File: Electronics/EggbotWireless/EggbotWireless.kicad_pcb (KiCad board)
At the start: 2 copper layers, 118 x 40 mm, 77 parts, among them J1 BATT, J2 Conn_01x03_Male, J3 USB_B_Micro, J4 AVR-ISP-6, J5 Conn_01x03_Female, J6 Conn_01x05_Male, M1 , M2 , M3 Motor_Servo, Q1 FDD8447L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

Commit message: fix some power issues
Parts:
- added C17: 10uF, Capacitor_SMD:C_0805_2012Metric_Pad1.15x1.40mm_HandSolder, F.Cu at (117.7, 60.9)
- added D4: SSB43L, Diode_SMD:D_SMB_Handsoldering, F.Cu at (113.2, 56.3)
- D1: value SK24 -> SSB43L
- D2: value SK84 -> SSB43L
- JP1, JP2, JP3: value (none) -> SolderJumper_2_Bridged; footprint Jumper:SolderJumper-2_P1.3mm_Open_Pad1.0x1.5mm -> Jumper:SolderJumper-2_P1.3mm_Bridged_Pad1.0x1.5mm
- Q1: value FDD8447L -> FDD8800
- Q3: value AOD403 -> IRLML6402; footprint Package_TO_SOT_SMD:TO-252-2 -> Package_TO_SOT_SMD:SOT-23
- R15: value 0.006 -> 0.008
- R16: value 9.1K -> 8.45K
- R20, R22, R6: value 100K -> 10K
- moved Q3 2.96 mm to (112.1, 60.8)
- moved D2 0.38 mm to (114.2, 47.2)
- moved JP2 0.05 mm to (43.1, 38.9)
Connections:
- Q3 pad 2: BATT -> Net-(D4-Pad1)
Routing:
- net Net-(D2-Pad1): track 27.2 -> 34.7 mm
- net BATT: track 57.9 -> 65.2 mm
- net VBUS: track 53.4 -> 60.4 mm
- net Net-(D4-Pad1): track 0.00 -> 4.29 mm, vias 0 -> 1
- net +5V: track 168.0 -> 169.9 mm, vias 2 -> 4
- net Net-(D1-Pad2): track 19.6 -> 20.1 mm, vias 1 -> 2
- net +12V: track 107.2 -> 107.7 mm, vias 0 -> 1
- net GND: vias 18 -> 19
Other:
- board text added: "Eggbot Wireless v1.3"
- board text removed: "Eggbot Wireless v1.2b"

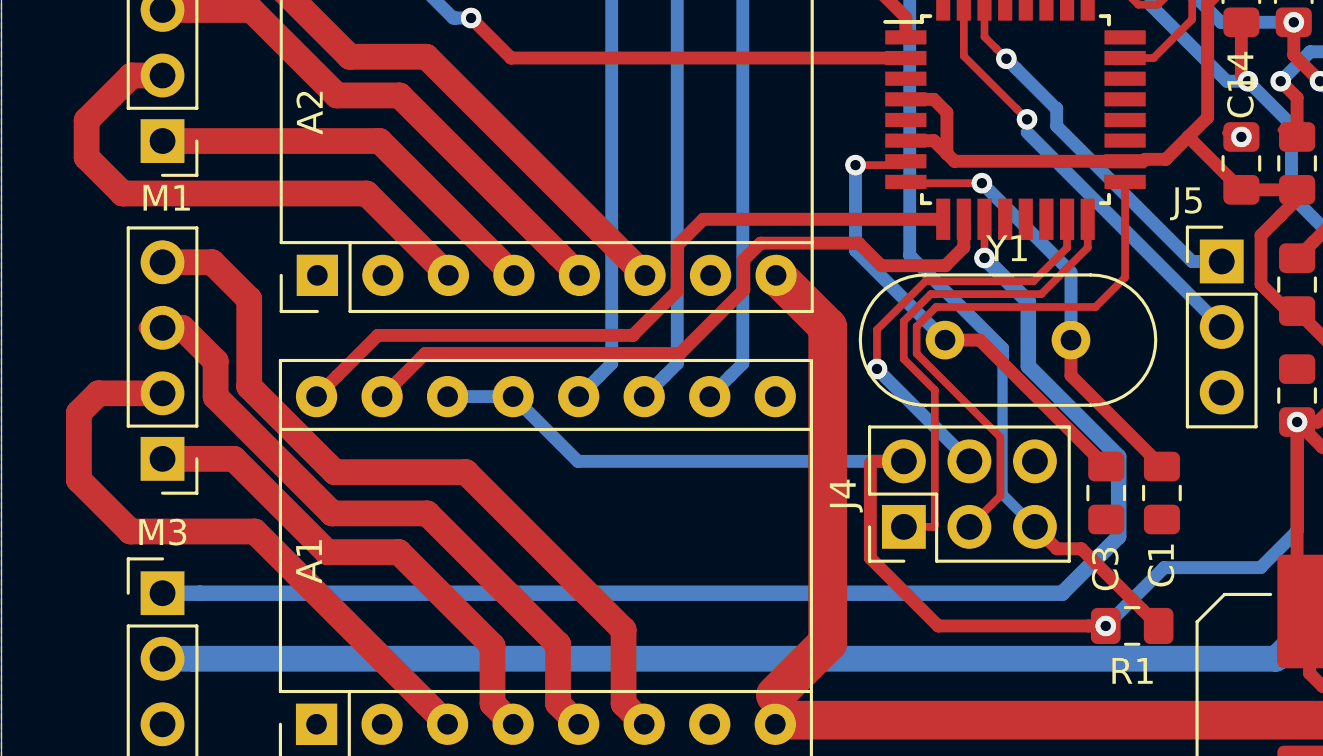
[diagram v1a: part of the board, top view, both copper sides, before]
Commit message: better crystal routing
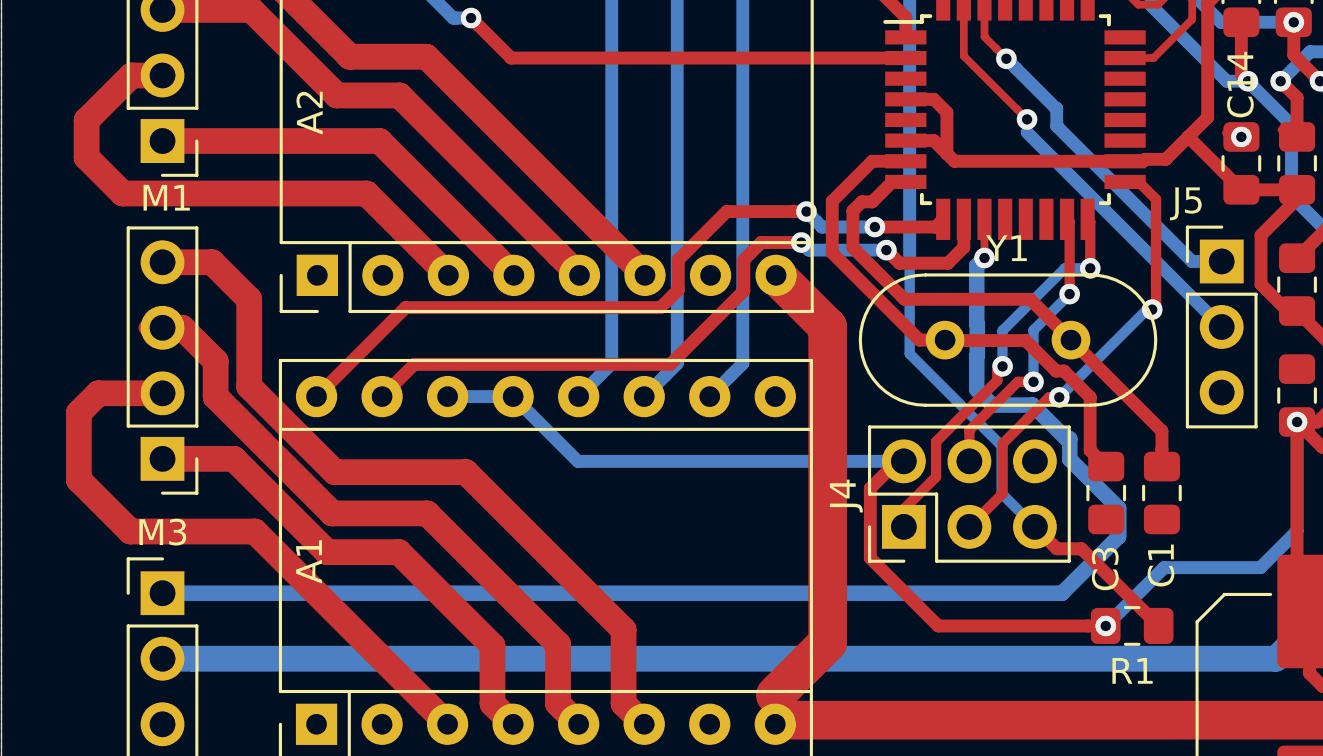
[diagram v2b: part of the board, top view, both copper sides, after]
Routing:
- net Net-(J4-Pad4): track 16.4 -> 11.4 mm, vias 1 -> 2
- net Net-(J4-Pad3): track 22.2 -> 17.5 mm, vias 0 -> 2
- net Net-(J4-Pad1): track 19.1 -> 15.5 mm, vias 0 -> 2
- net Net-(C1-Pad1): track 16.8 -> 20.2 mm, vias 1 -> 0
- net Net-(C3-Pad2): track 18.5 -> 20.8 mm, vias 1 -> 0
- net Net-(M3-Pad1): track 52.4 -> 53.7 mm
- net +3V3: track 246.0 -> 245.4 mm
- net DIR1: track 28.2 -> 28.3 mm, vias 0 -> 2
- net STEP1: vias 0 -> 2

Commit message: board v1.3
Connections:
- A1 pad 2: (no net) -> Net-(A1-Pad2)
- A1 pad 9: (no net) -> Net-(A1-Pad9)
- A2 pad 2: (no net) -> Net-(A2-Pad2)
- A2 pad 9: (no net) -> Net-(A2-Pad9)
- J3 pad 4: (no net) -> Net-(J3-Pad4)
- SW1 pad 3: (no net) -> Net-(SW1-Pad3)
- U2 pad 12: (no net) -> Net-(U2-Pad12)
- U2 pad 13: (no net) -> Net-(U2-Pad13)
- U2 pad 14: (no net) -> Net-(U2-Pad14)
- U2 pad 19: (no net) -> Net-(U2-Pad19)
- U2 pad 20: (no net) -> Net-(U2-Pad20)
- U2 pad 22: (no net) -> Net-(U2-Pad22)
- U2 pad 24: (no net) -> Net-(U2-Pad24)
- U2 pad 25: (no net) -> Net-(U2-Pad25)
- U2 pad 26: (no net) -> Net-(U2-Pad26)
- U2 pad 32: (no net) -> Net-(U2-Pad32)
- U3 pad 4: (no net) -> Net-(U3-Pad4)
- U5 pad 10: (no net) -> Net-(U5-Pad10)
- U5 pad 11: (no net) -> Net-(U5-Pad11)
- U5 pad 13: (no net) -> Net-(U5-Pad13)
- U5 pad 14: (no net) -> Net-(U5-Pad14)
- U5 pad 19: (no net) -> Net-(U5-Pad19)
- U5 pad 22: (no net) -> Net-(U5-Pad22)
- U5 pad 23: (no net) -> Net-(U5-Pad23)
- U5 pad 27: (no net) -> Net-(U5-Pad27)
- U5 pad 28: (no net) -> Net-(U5-Pad28)
- U5 pad 6: (no net) -> Net-(U5-Pad6)
- U5 pad 9: (no net) -> Net-(U5-Pad9)
- U7 pad 10: (no net) -> Net-(U7-Pad10)
- U7 pad 11: (no net) -> Net-(U7-Pad11)
- U7 pad 12: (no net) -> Net-(U7-Pad12)
- U7 pad 13: (no net) -> Net-(U7-Pad13)
- U7 pad 14: (no net) -> Net-(U7-Pad14)
- U7 pad 4: (no net) -> Net-(U7-Pad4)
- U7 pad 5: (no net) -> Net-(U7-Pad5)
- U7 pad 9: (no net) -> Net-(U7-Pad9)

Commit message: make inductor 6.8uH
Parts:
- L1: value 3.3uH -> 6.8uH
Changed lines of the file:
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@@
       (effects (font (size 1 1) (thickness 0.15)))
     )
-    (fp_text value 3.3uH (at 0 4.45) (layer F.Fab)
+    (fp_text value 6.8uH (at 0 4.45) (layer F.Fab)
       (effects (font (size 1 1) (thickness 0.15)))
     )

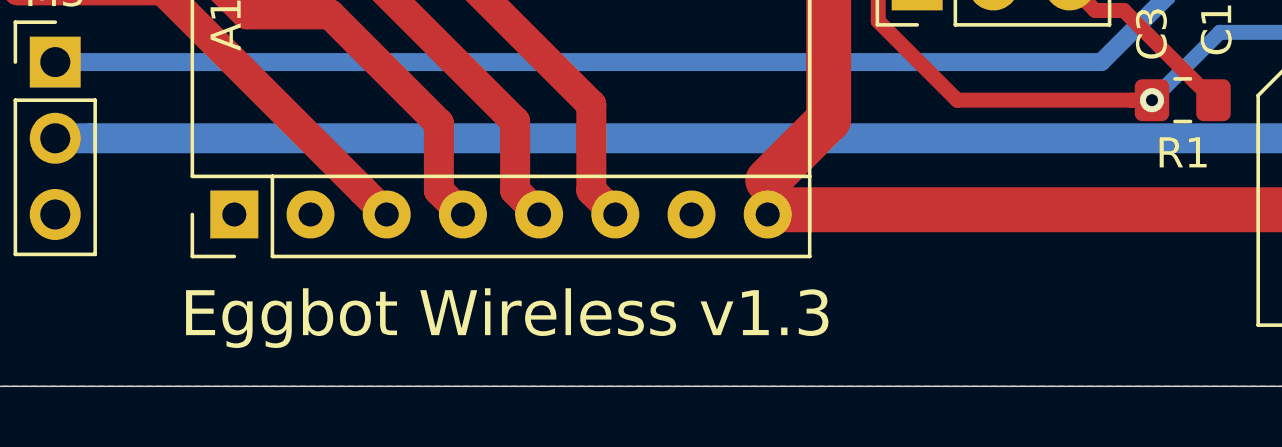
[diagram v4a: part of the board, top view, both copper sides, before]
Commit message: v1.3f some changes to the schematic
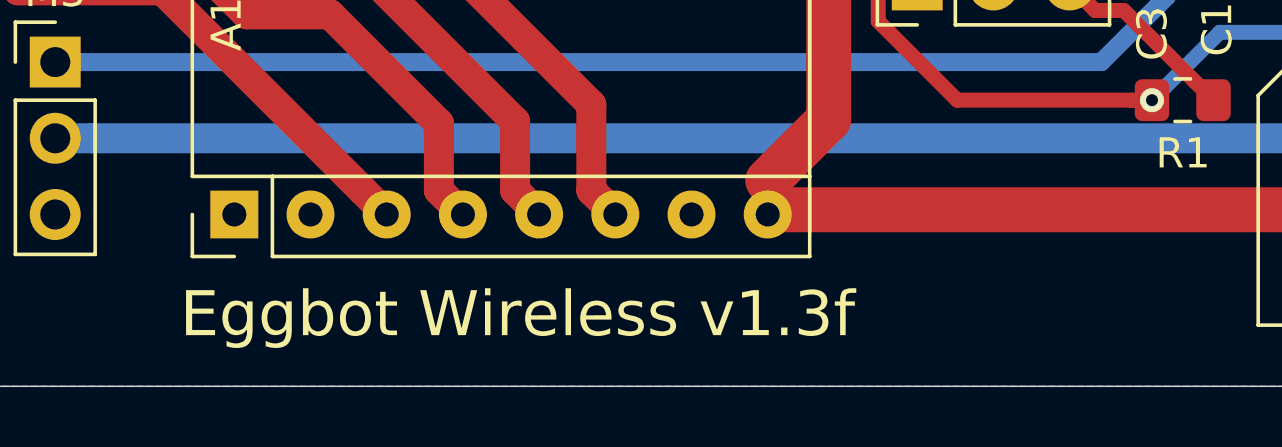
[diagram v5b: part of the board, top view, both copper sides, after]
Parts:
- R21: value 330 -> 510
- R27: value 3K -> 2.2K
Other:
- board text added: "Eggbot Wireless v1.3f"
- board text removed: "Eggbot Wireless v1.3"
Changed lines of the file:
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@@
-(kicad_pcb (version 20171130) (host pcbnew 5.1.2-5.1.2)
+(kicad_pcb (version 20171130) (host pcbnew 5.1.2-1.fc30)
   (general
     (thickness 1.6)
@@
       (effects (font (size 1 1) (thickness 0.15)))
     )
-    (fp_text value 3K (at 0 1.65 90) (layer F.Fab)
+    (fp_text value 2.2K (at 0 1.65 90) (layer F.Fab)
       (effects (font (size 1 1) (thickness 0.15)))
     )
@@
       (effects (font (size 1 1) (thickness 0.15)))
     )
-    (fp_text value 330 (at 0 1.65) (layer F.Fab)
+    (fp_text value 510 (at 0 1.65) (layer F.Fab)
       (effects (font (size 1 1) (thickness 0.15)))
     )
@@
   (gr_line (start 137.364 37.528) (end 137.364 77.528) (layer Edge.Cuts) (width 0.05))
   (gr_line (start 19.364 37.528) (end 137.364 37.528) (layer Edge.Cuts) (width 0.05))
-  (gr_text "Eggbot Wireless v1.3" (at 29.764 75.128) (layer F.SilkS)
+  (gr_text "Eggbot Wireless v1.3f" (at 29.764 75.128) (layer F.SilkS)
     (effects (font (size 1.5 1.5) (thickness 0.3)) (justify left))
   )

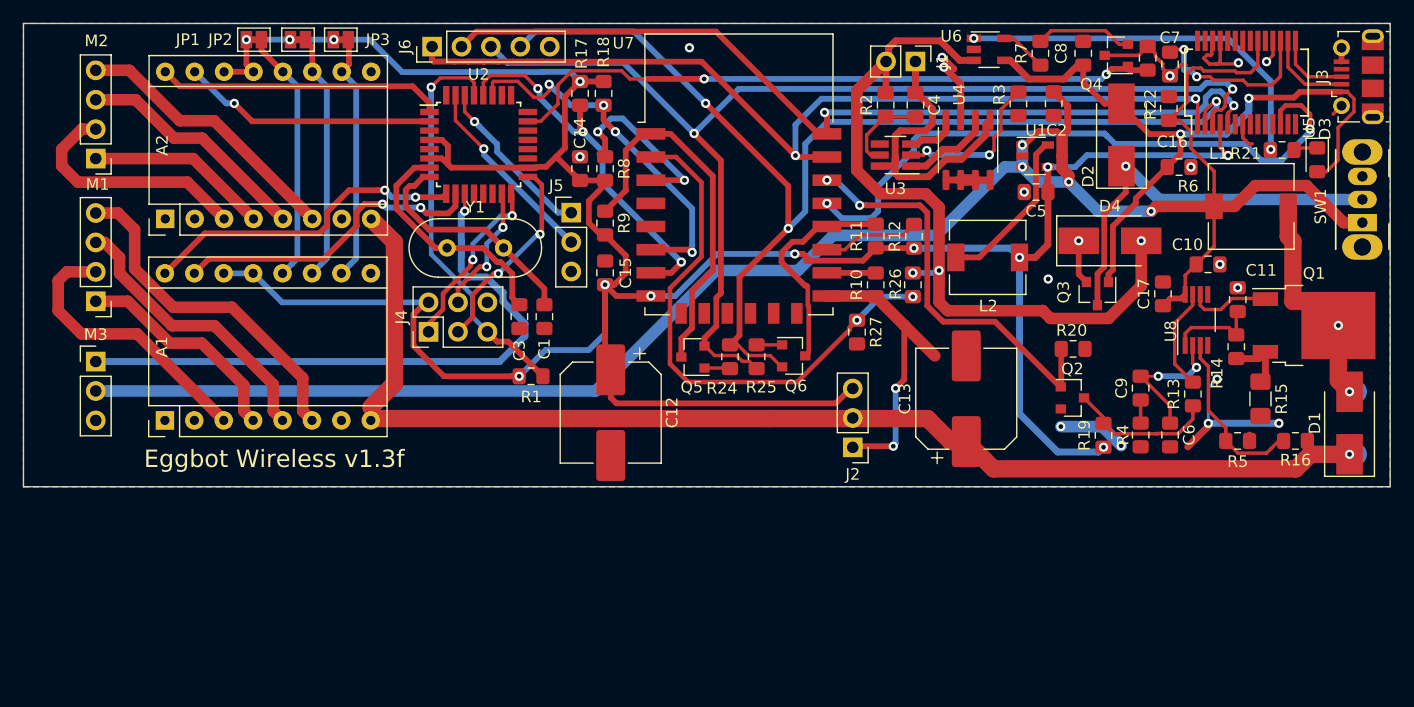
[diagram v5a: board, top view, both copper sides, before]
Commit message: add 5v boost schematic
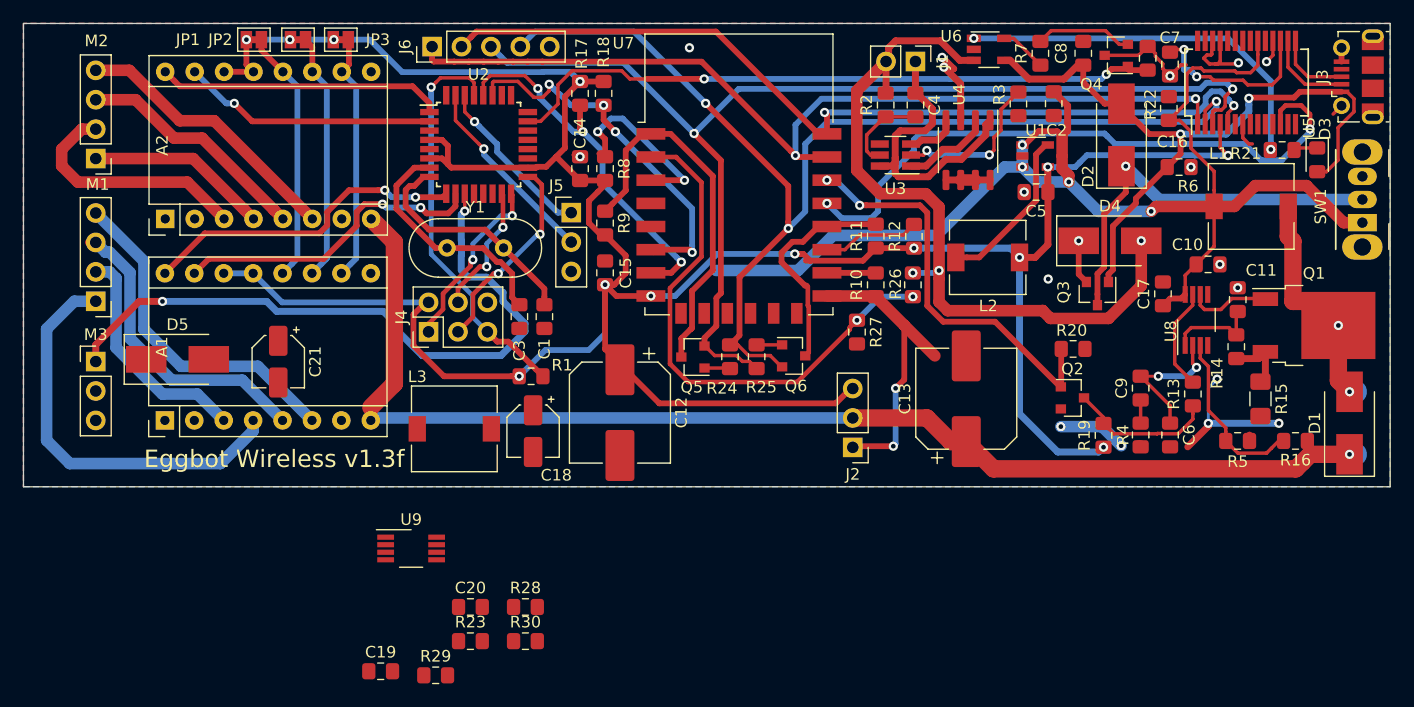
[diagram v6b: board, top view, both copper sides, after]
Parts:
- added C18: 10uF, Capacitor_SMD:CP_Elec_4x5.4, F.Cu at (63.4, 72.7)
- added C19: 22pF, Capacitor_SMD:C_0805_2012Metric_Pad1.15x1.40mm_HandSolder, F.Cu at (50.2, 93.5)
- added C20: 100nF, Capacitor_SMD:C_0805_2012Metric_Pad1.15x1.40mm_HandSolder, F.Cu at (58.0, 87.9)
- added C21: 10uF, Capacitor_SMD:CP_Elec_4x5.4, F.Cu at (41.4, 66.7)
- added D5: SSB43L, Diode_SMD:D_SMB_Handsoldering, F.Cu at (32.7, 66.5)
- added L3: 6.8uH, Inductor_SMD:L_7.3x7.3_H4.5, F.Cu at (56.6, 72.5)
- added R23: 50K, Resistor_SMD:R_0805_2012Metric_Pad1.15x1.40mm_HandSolder, F.Cu at (58.0, 90.9)
- added R28: 150K, Resistor_SMD:R_0805_2012Metric_Pad1.15x1.40mm_HandSolder, F.Cu at (62.7, 87.9)
- added R29: 200K, Resistor_SMD:R_0805_2012Metric_Pad1.15x1.40mm_HandSolder, F.Cu at (55.0, 93.8)
- added R30: 500, Resistor_SMD:R_0805_2012Metric_Pad1.15x1.40mm_HandSolder, F.Cu at (62.7, 90.9)
- added U9: LM2621, Package_SO:VSSOP-8_3.0x3.0mm_P0.65mm, F.Cu at (52.8, 82.9)
- moved C12 0.80 mm to (70.9, 71.1)
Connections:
- net 12V_SWITCH renamed PWR_SWITCH
- A1 pad 2: Net-(A1-Pad2) -> (no net)
- A1 pad 9: Net-(A1-Pad9) -> (no net)
- A2 pad 2: Net-(A2-Pad2) -> (no net)
- A2 pad 9: Net-(A2-Pad9) -> (no net)
- J3 pad 4: Net-(J3-Pad4) -> (no net)
- M3 pad 2: +5V -> SERVOPWR
- SW1 pad 3: Net-(SW1-Pad3) -> (no net)
- U2 pad 12: Net-(U2-Pad12) -> (no net)
- U2 pad 13: Net-(U2-Pad13) -> (no net)
- U2 pad 14: Net-(U2-Pad14) -> (no net)
- U2 pad 19: Net-(U2-Pad19) -> (no net)
- U2 pad 20: Net-(U2-Pad20) -> (no net)
- U2 pad 22: Net-(U2-Pad22) -> (no net)
- U2 pad 24: Net-(U2-Pad24) -> (no net)
- U2 pad 25: Net-(U2-Pad25) -> (no net)
- U2 pad 26: Net-(U2-Pad26) -> (no net)
- U2 pad 32: Net-(U2-Pad32) -> (no net)
- U3 pad 4: Net-(U3-Pad4) -> (no net)
- U5 pad 10: Net-(U5-Pad10) -> (no net)
- U5 pad 11: Net-(U5-Pad11) -> (no net)
- U5 pad 13: Net-(U5-Pad13) -> (no net)
- U5 pad 14: Net-(U5-Pad14) -> (no net)
- U5 pad 19: Net-(U5-Pad19) -> (no net)
- U5 pad 22: Net-(U5-Pad22) -> (no net)
- U5 pad 23: Net-(U5-Pad23) -> (no net)
- U5 pad 27: Net-(U5-Pad27) -> (no net)
- U5 pad 28: Net-(U5-Pad28) -> (no net)
- U5 pad 6: Net-(U5-Pad6) -> (no net)
- U5 pad 9: Net-(U5-Pad9) -> (no net)
- U7 pad 10: Net-(U7-Pad10) -> (no net)
- U7 pad 11: Net-(U7-Pad11) -> (no net)
- U7 pad 12: Net-(U7-Pad12) -> (no net)
- U7 pad 13: Net-(U7-Pad13) -> (no net)
- U7 pad 14: Net-(U7-Pad14) -> (no net)
- U7 pad 4: Net-(U7-Pad4) -> (no net)
- U7 pad 5: Net-(U7-Pad5) -> (no net)
- U7 pad 9: Net-(U7-Pad9) -> (no net)
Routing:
- net +5V: track 169.9 -> 112.0 mm
- net Net-(A1-Pad4): track 19.2 -> 35.6 mm
- net Net-(M3-Pad1): track 53.7 -> 58.4 mm, vias 1 -> 2
- net Net-(A1-Pad3): track 24.4 -> 19.9 mm
- net +3V3: track 245.4 -> 243.3 mm
- net Net-(A1-Pad5): track 25.2 -> 26.3 mm

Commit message: v1.4 beta board (added a 5v boost converter to the board)
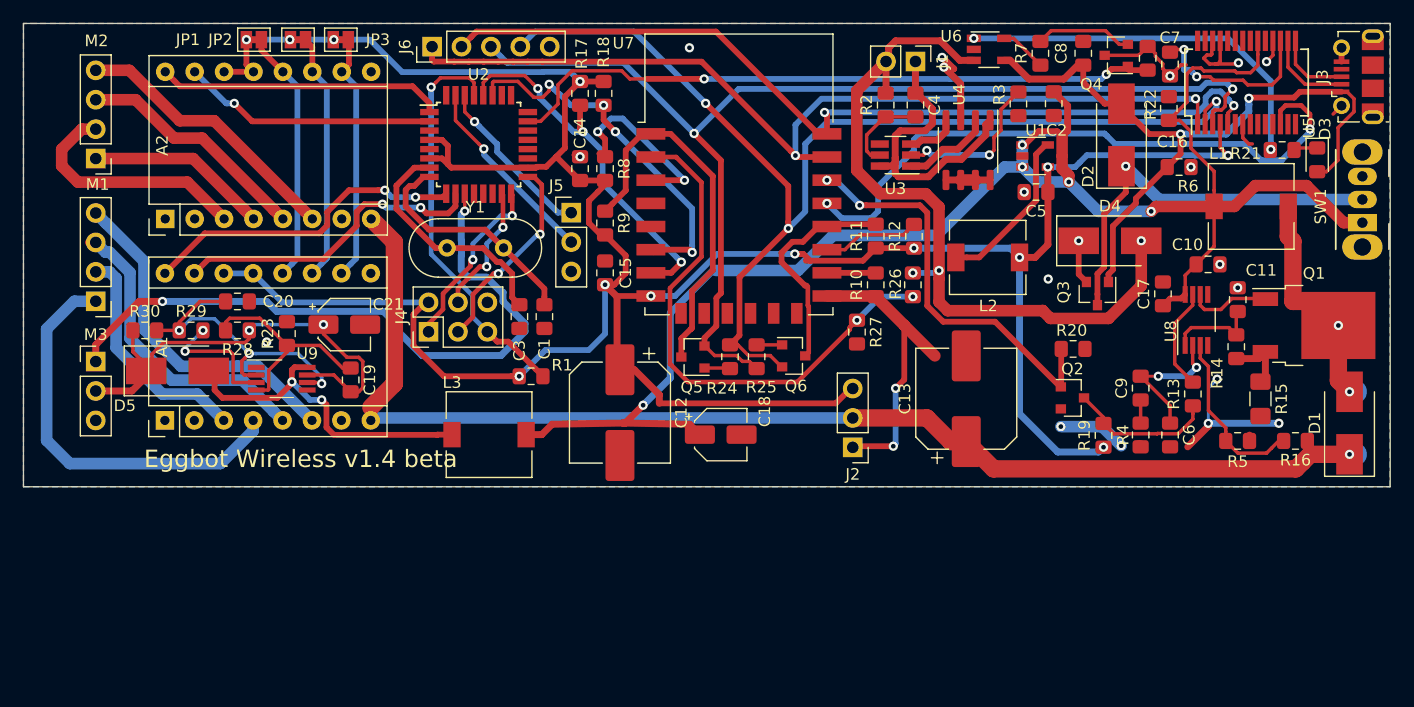
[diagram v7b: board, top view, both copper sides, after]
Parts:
- moved R30 42.4 mm to (29.8, 64.0)
- moved R29 36.5 mm to (33.8, 64.0)
- moved R28 34.5 mm to (37.8, 64.0), turned to 180 degrees
- moved C20 33.2 mm to (37.8, 61.5)
- moved R23 30.9 mm to (42.1, 64.3), turned to 90 degrees
- moved C19 25.3 mm to (47.6, 68.3), turned to 270 degrees
- moved U9 18.4 mm to (41.7, 68.2)
- moved C18 16.2 mm to (79.6, 73.0), turned to 0 degrees
- moved C21 6.54 mm to (47.1, 63.5), turned to 0 degrees
- moved L3 3.04 mm to (59.6, 73.0)
- moved D5 1.00 mm to (32.7, 67.5)
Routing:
- net SERVOPWR: track 0.00 -> 40.5 mm, vias 0 -> 2
- net +5V: track 112.0 -> 144.6 mm, vias 4 -> 5
- net Net-(D5-Pad2): track 0.00 -> 28.7 mm, vias 0 -> 2
- net Net-(C20-Pad1): track 0.00 -> 27.3 mm, vias 0 -> 3
- net Net-(C19-Pad1): track 0.00 -> 19.0 mm
- net Net-(R29-Pad2): track 0.00 -> 11.1 mm, vias 0 -> 2
- net +3V3: track 243.3 -> 244.0 mm
- net GND: vias 19 -> 20
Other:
- board text added: "Eggbot Wireless v1.4 beta"
- board text removed: "Eggbot Wireless v1.3f"
